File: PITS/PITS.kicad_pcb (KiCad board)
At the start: 2 copper layers, 65 x 30 mm, 47 parts, among them P1 CONN_02X20, P14 BATT, P2 BNC, P3 BNC, P4 BNC, P5 BNC, P6 Batt, P7 SENSOR, Q1 Q_PMOS_DGS, Q2 Q_PNP_dual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

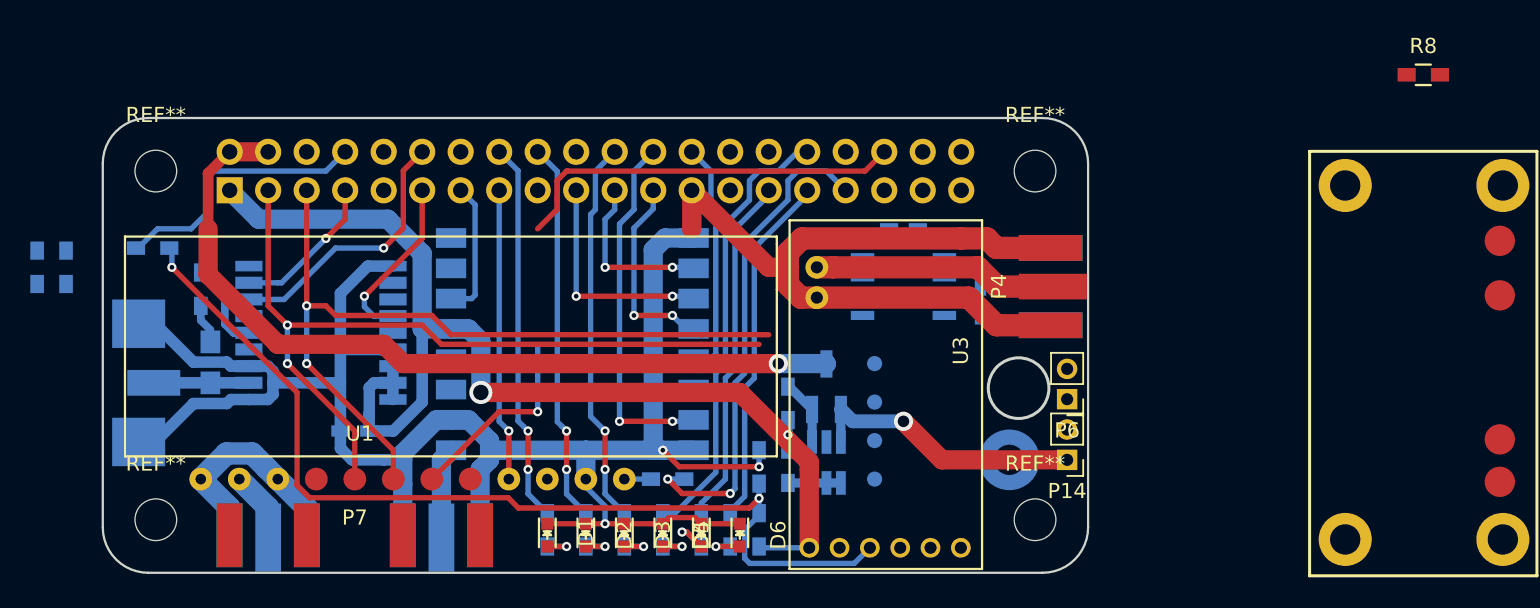
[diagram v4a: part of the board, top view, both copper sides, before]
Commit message: PCB save befor rerouting power lines
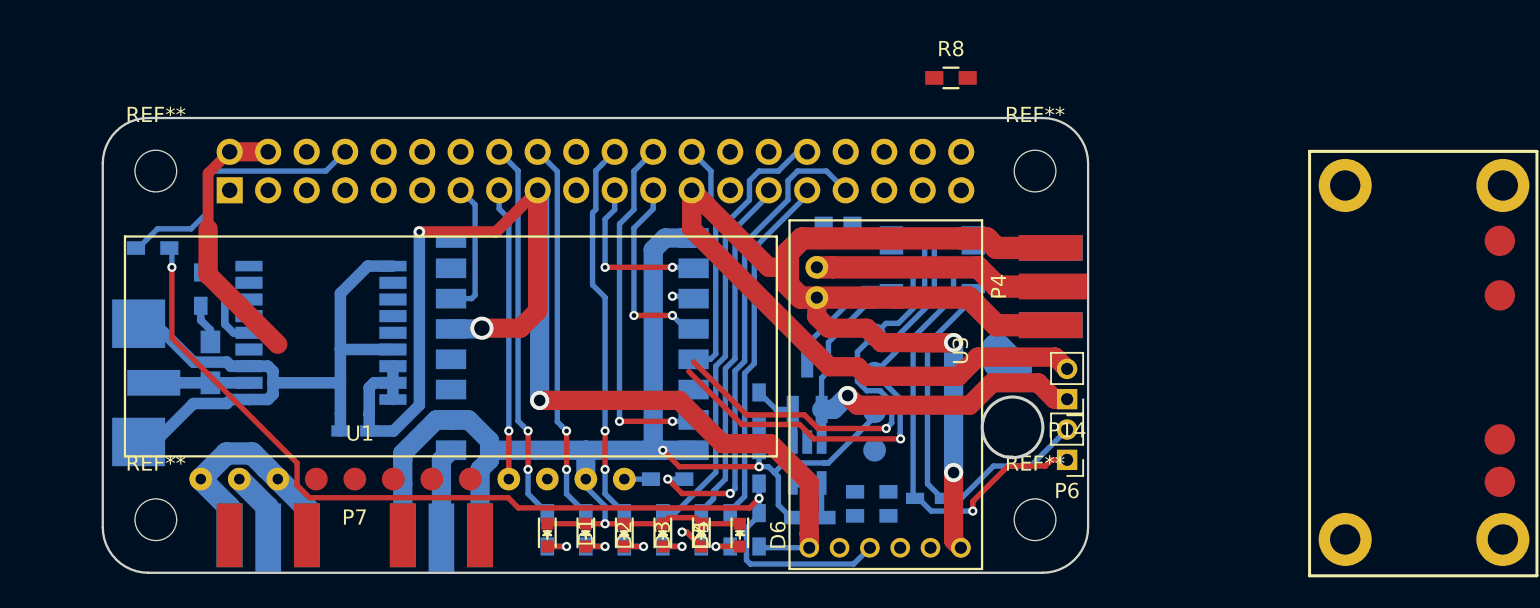
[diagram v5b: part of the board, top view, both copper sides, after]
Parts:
- moved R24 57.4 mm to (105.7, 75.2), turned to 180 degrees
- moved R25 55.2 mm to (105.7, 73.7), turned to 0 degrees
- moved R8 31.2 mm to (111.0, 46.4)
- moved C2 13.4 mm to (109.5, 74.1), turned to 0 degrees
- moved U8 11.1 mm to (104.4, 61.9)
- moved C1 4.34 mm to (103.5, 55.9), turned to 180 degrees
- moved P14 4.00 mm to (118.6, 67.5)
- moved P6 4.00 mm to (118.6, 71.5)
- moved R6 3.68 mm to (101.6, 75.4), turned to 180 degrees
- moved U7 2.61 mm to (109.7, 58.3)
- moved R19 1.94 mm to (98.3, 68.2)
- moved Q1 1.27 mm to (101.5, 66.7)
- moved Q2 1.27 mm to (101.5, 71.7)
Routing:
- net GND: track 193.9 -> 258.3 mm, vias 4 -> 5
- net /GPIO16(CE2): track 39.4 -> 0.00 mm, vias 1 -> 0
- net Net-(C2-Pad1): track 0.00 -> 29.6 mm, vias 0 -> 1
- net I_neg: track 54.5 -> 26.1 mm, vias 1 -> 0
- net Net-(C2-Pad2): track 0.00 -> 25.6 mm
- net /GPIO2(SDA1): track 53.1 -> 33.3 mm, vias 2 -> 1
- net /GPIO3(SCL1): track 52.7 -> 34.0 mm, vias 2 -> 1
- net /GPIO18: track 17.7 -> 0.00 mm, vias 1 -> 0
- net I_pos: track 18.5 -> 34.5 mm
- net /GPIO10(MOSI0): track 14.8 -> 1.46 mm, vias 2 -> 1
- net /GPIO17: track 11.4 -> 0.00 mm, vias 1 -> 0
- net +3V3: track 75.6 -> 86.9 mm, vias 1 -> 3
- net /GPIO4: track 9.99 -> 0.00 mm, vias 1 -> 0
- net Net-(Q2-Pad1): track 3.49 -> 4.32 mm

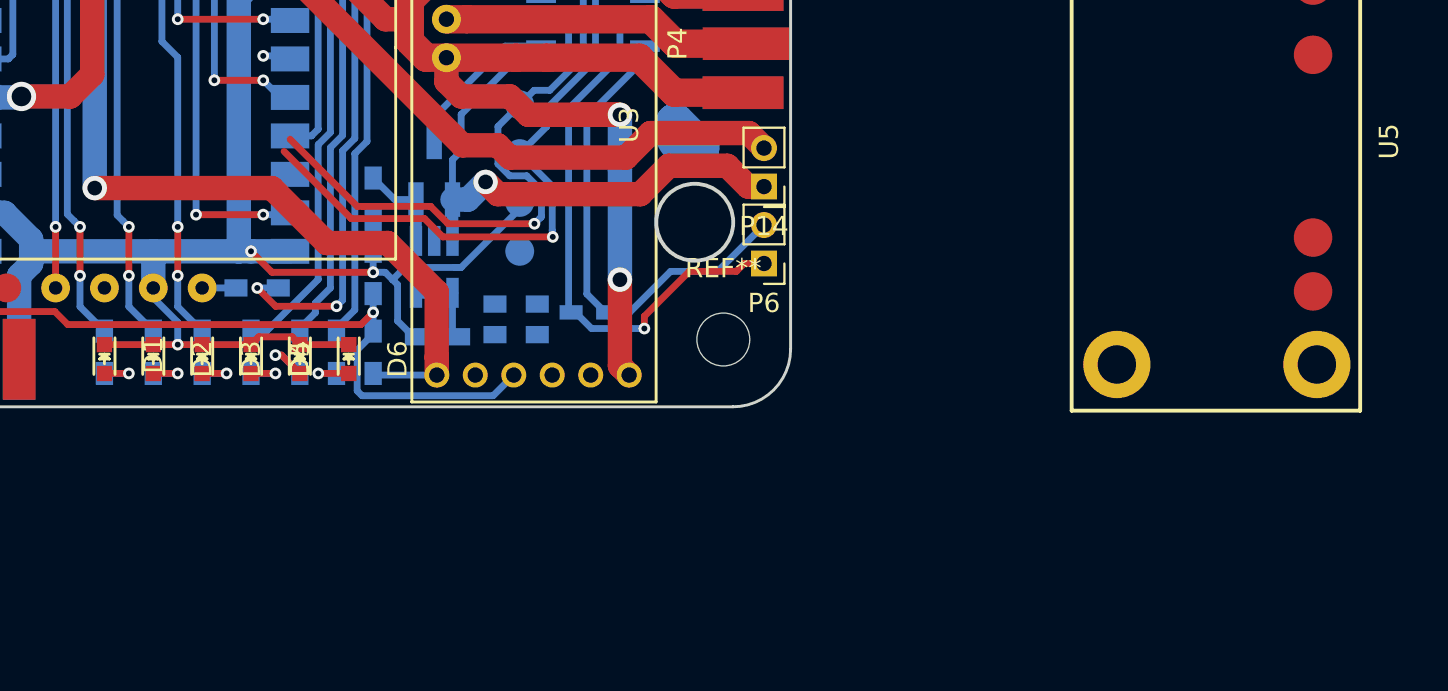
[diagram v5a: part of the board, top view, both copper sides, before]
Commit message: removed scound LORA led
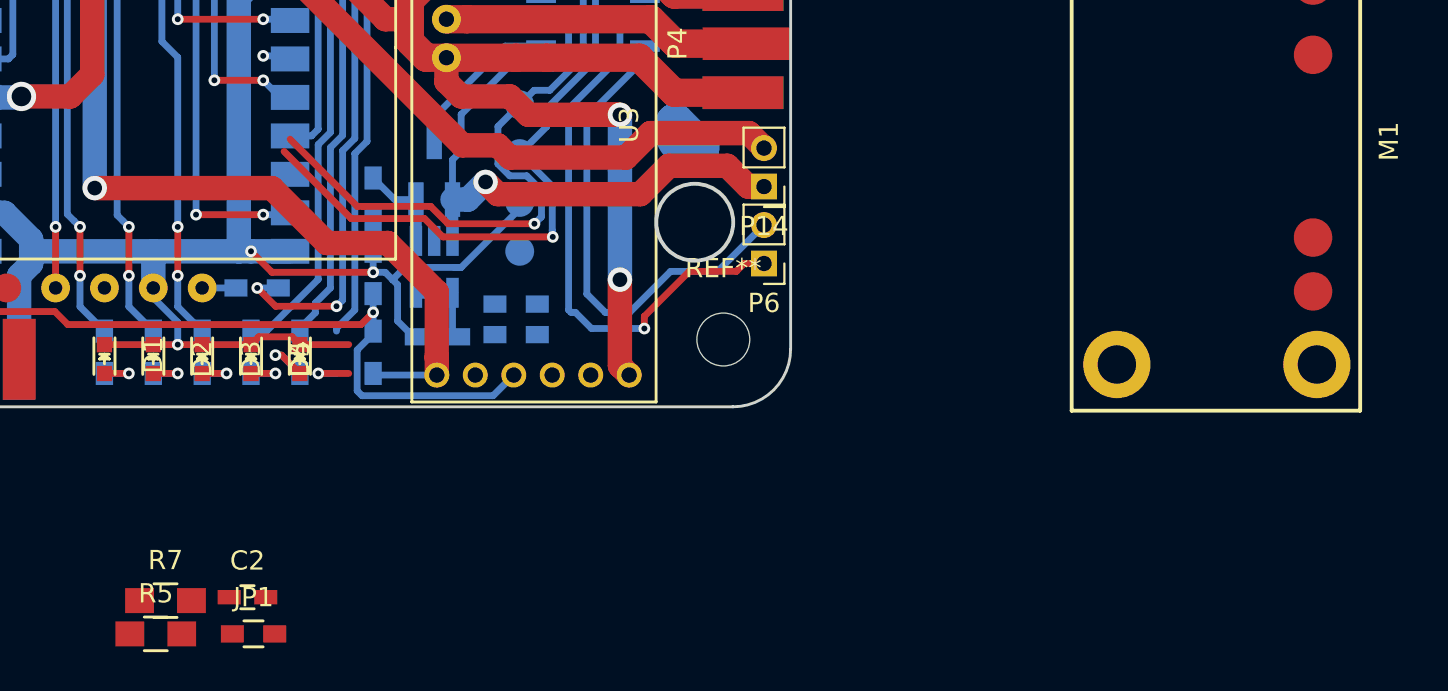
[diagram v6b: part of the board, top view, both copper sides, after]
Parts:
- removed D6: DATA1_Red, LEDs:LED_0603
- removed R23: 330, Resistors_SMD:R_0603_HandSoldering
- added JP1: CH2- to GND, Resistors_SMD:R_0603_HandSoldering, F.Cu at (92.1, 90.8)
- added R5: 15k, Resistors_SMD:R_0805_HandSoldering, F.Cu at (87.0, 90.8)
- added R7: 10k, Resistors_SMD:R_0805_HandSoldering, F.Cu at (87.5, 89.1)
- C2: moved to F.Cu
- D5: value DATA0_Red -> LORA_Red
- R26: value 10k -> 20k
- moved C2 23.1 mm to (91.8, 88.9)
- renumbered U5 to M1, U8 to M2
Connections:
- P6 pad 1: Net-(C2-Pad1) -> Net-(P6-Pad1)
- U2 pad 6: GND -> +3V3
- U7 pad 1: I_neg -> I_pos
- U7 pad 2: I_pos -> I_neg
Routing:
- net GND: track 258.3 -> 237.4 mm
- net +3V3: track 86.9 -> 107.8 mm
- net Net-(P6-Pad1): track 0.00 -> 7.99 mm, vias 0 -> 1
- net Net-(C2-Pad1): track 29.6 -> 21.6 mm, vias 1 -> 0
- net I_pos: track 34.5 -> 40.4 mm
- net I_neg: track 26.1 -> 20.2 mm
- net /D6: track 2.53 -> 0.00 mm, vias 1 -> 0
- net (no net): track 0.00 -> 2.53 mm, vias 0 -> 1

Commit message: PCB save
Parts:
- P7: footprint Connectors:SMD_5_xsmall -> Pin_Headers:Pin_Header_Straight_1x05_Pitch2.54mm
- moved R3 36.1 mm to (76.2, 88.9)
- moved D1 25.1 mm to (77.3, 100.6)
- moved D2 25.1 mm to (79.9, 100.6)
- moved D3 25.1 mm to (82.4, 100.6)
- moved D4 25.1 mm to (85.0, 100.6)
- moved D5 25.1 mm to (87.5, 100.6)
- moved R14 25.1 mm to (77.3, 100.3)
- moved R15 25.1 mm to (79.9, 100.3)
- moved R20 25.1 mm to (82.4, 100.3)
- moved R21 25.1 mm to (85.0, 100.3)
- moved R22 25.1 mm to (87.5, 100.3)
- moved P7 15.6 mm to (84.3, 76.0), turned to 90 degrees
- moved C14 13.1 mm to (74.8, 56.9)
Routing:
- net /MTX2-TXD: track 64.6 -> 0.15 mm, vias 2 -> 0
- net +3V3: track 107.8 -> 46.4 mm, vias 3 -> 0
- net /GPIO3(SCL1): track 34.0 -> 0.01 mm, vias 1 -> 0
- net /GPIO2(SDA1): track 33.3 -> 0.00 mm, vias 1 -> 0
- net /GPIO13: track 32.4 -> 0.00 mm, vias 2 -> 0
- net /GPIO12: track 29.4 -> 0.64 mm
- net Net-(C2-Pad2): track 25.6 -> 0.00 mm
- net /GPIO25: track 25.3 -> 0.00 mm, vias 2 -> 0
- net /GPIO24: track 25.2 -> 0.00 mm, vias 2 -> 0
- net /GPIO23: track 25.2 -> 0.00 mm, vias 2 -> 0
- net /GPIO8(CE0): track 23.6 -> 0.13 mm, vias 2 -> 0
- net /GPIO6: track 23.4 -> 0.32 mm
- net /GPIO5: track 23.1 -> 0.47 mm
- net Net-(C2-Pad1): track 21.6 -> 0.00 mm
- net /GPIO22: track 19.3 -> 0.00 mm, vias 1 -> 0
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
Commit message: all power routing done
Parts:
- C2, JP1, P4, R5, R7, R8: moved to B.Cu
- P14, P6: footprint Pin_Headers:Pin_Header_Straight_1x02_Pitch2.00mm -> Connectors:SMD_2_xsmall; moved to B.Cu
- P7: footprint Pin_Headers:Pin_Header_Straight_1x05_Pitch2.54mm -> Connectors:SMD_5_xsmall; moved to B.Cu
- moved M2 61.6 mm to (166.0, 60.0)
- moved R3 32.5 mm to (73.0, 56.5)
- moved R7 28.6 mm to (107.8, 69.0)
- moved JP1 28.5 mm to (107.8, 67.1), turned to 180 degrees
- moved R5 28.4 mm to (107.8, 71.5), turned to 180 degrees
- moved D5 26.7 mm to (98.9, 76.5)
- moved D4 26.2 mm to (95.1, 76.5)
- moved D3 25.7 mm to (91.3, 76.5)
- moved D2 25.3 mm to (87.5, 76.5)
- moved R14 25.0 mm to (83.1, 76.0)
- moved D1 25.0 mm to (83.7, 76.5)
- moved R15 24.8 mm to (85.0, 76.0)
- moved R20 24.7 mm to (86.9, 76.0)
- moved R21 24.6 mm to (88.8, 76.0)
- moved R22 24.5 mm to (90.7, 76.0)
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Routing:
- net I_neg: track 36.6 -> 104.7 mm, vias 0 -> 3
- net GND: track 251.9 -> 206.7 mm, vias 1 -> 62
- net /MTX2-TXD: track 0.15 -> 17.4 mm
- net +3V3: track 46.4 -> 29.4 mm, vias 0 -> 4
- net Net-(C2-Pad2): track 0.00 -> 14.5 mm
- net /GPIO3(SCL1): track 0.01 -> 10.6 mm
- net /D5: track 0.00 -> 9.30 mm, vias 0 -> 1
- net /D4: track 0.00 -> 7.96 mm, vias 0 -> 1
- net /D3: track 0.00 -> 6.97 mm, vias 0 -> 1
- net Net-(C2-Pad1): track 0.00 -> 6.92 mm
- net /GPIO2(SDA1): track 0.00 -> 5.65 mm
- net Net-(Q1-Pad2): track 4.84 -> 9.03 mm
- net /D2: track 0.00 -> 4.15 mm, vias 0 -> 1
- net Net-(Q2-Pad1): track 1.90 -> 5.21 mm
- net /D1: track 0.00 -> 3.25 mm, vias 0 -> 1
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- added copper zone on In1.Cu, net +3V3
- added copper zone on In2.Cu, net GND
- added copper zone on F.Cu, net I_neg
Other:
- copper layers 2 -> 4
- rule pad_to_mask_clearance: 0.2 -> 0.0381
- rule trace_min: 0.2032 -> 0.127
- rule via_min_drill: 0.3048 -> 0.254
- rule via_min_size: 0.6096 -> 0.4572
- board text added: "3V3"
- board text added: "GND"
